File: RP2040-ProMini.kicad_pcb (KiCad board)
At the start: 2 copper layers, 17.8 x 33 mm, 6 parts, among them J1 CONN_L, J2 CONN_R, J3 CONN_R2, J4 CONN_R3, J5 CONN_U, U1 RP2040

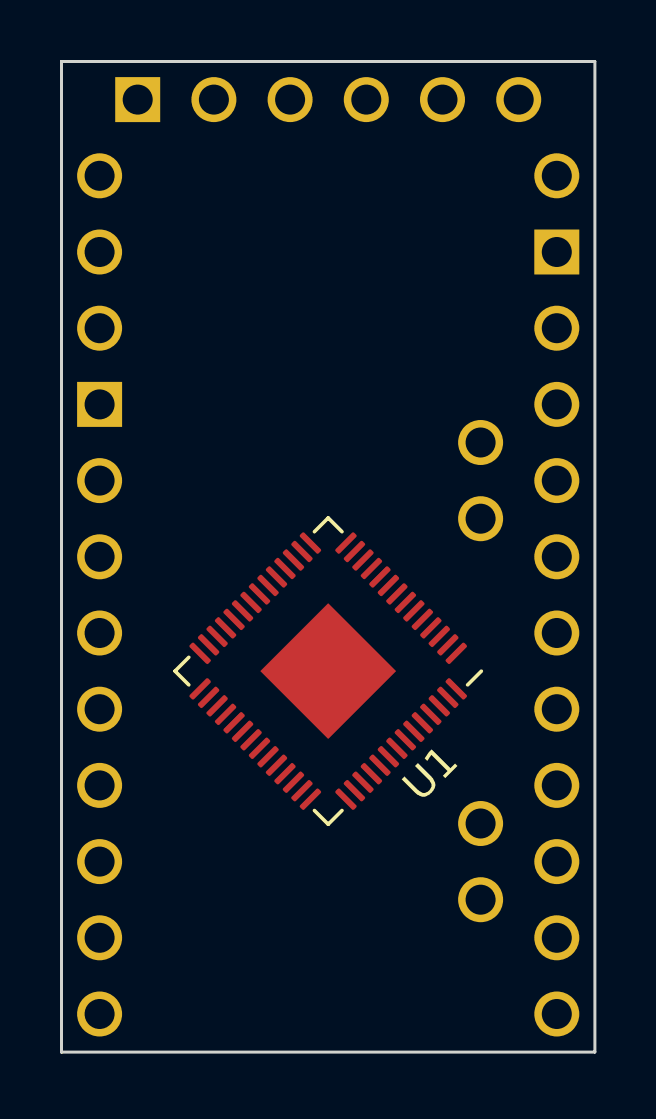
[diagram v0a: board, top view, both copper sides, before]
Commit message: Added basic power input
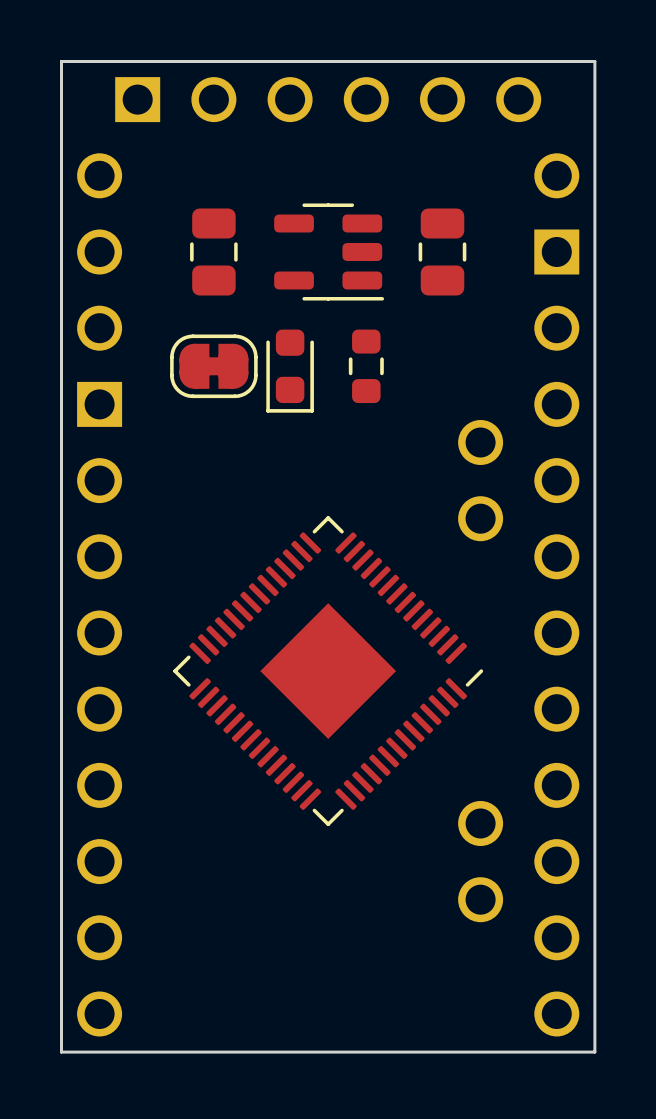
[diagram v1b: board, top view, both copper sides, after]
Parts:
- added C1: 10uF, Capacitor_SMD:C_0805_2012Metric, F.Cu at (160.0, 100.3)
- added C2: 10uF, Capacitor_SMD:C_0805_2012Metric, F.Cu at (152.4, 100.3)
- added D1: RED, LED_SMD:LED_0603_1608Metric, F.Cu at (154.9, 104.1)
- added JP1: EXT_POWER, Jumper:SolderJumper-2_P1.3mm_Bridged_RoundedPad1.0x1.5mm, F.Cu at (152.4, 104.1)
- added R1: 10k, Resistor_SMD:R_0603_1608Metric, F.Cu at (157.5, 104.1)
- added U2: MIC5205-3.3YM5, Package_TO_SOT_SMD:SOT-23-5, F.Cu at (156.2, 100.3)

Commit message: Added whole bunch of things
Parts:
- added C10: 100nF, Capacitor_SMD:C_0402_1005Metric, F.Cu at (151.1, 110.5)
- added C11: 2.2uF, Capacitor_SMD:C_0603_1608Metric, F.Cu at (158.7, 119.4)
- added C12: 2.2uF, Capacitor_SMD:C_0603_1608Metric, F.Cu at (151.1, 123.2)
- added C3: 100nF, Capacitor_SMD:C_0402_1005Metric, F.Cu at (151.1, 125.7)
- added C4: 100nF, Capacitor_SMD:C_0402_1005Metric, F.Cu at (157.5, 106.7)
- added C5: 100nF, Capacitor_SMD:C_0402_1005Metric, F.Cu at (151.1, 109.2)
- added C6: 100nF, Capacitor_SMD:C_0402_1005Metric, F.Cu at (157.5, 120.7)
- added C7: 100nF, Capacitor_SMD:C_0402_1005Metric, F.Cu at (156.2, 120.7)
- added C8: 100nF, Capacitor_SMD:C_0402_1005Metric, F.Cu at (151.1, 115.6)
- added C9: 100nF, Capacitor_SMD:C_0402_1005Metric, F.Cu at (158.8, 106.7)
- added D2: RED, LED_SMD:LED_0603_1608Metric, F.Cu at (152.4, 120.7)
- added Q1: AO3400A, Package_TO_SOT_SMD:SOT-23, F.Cu at (152.4, 118.1)
- added R2: 10k, Resistor_SMD:R_0402_1005Metric, F.Cu at (158.8, 102.9)
- added R3: 10k, Resistor_SMD:R_0402_1005Metric, F.Cu at (160.0, 102.9)
- added R4: 10k, Resistor_SMD:R_0402_1005Metric, F.Cu at (161.3, 102.9)
- added R5: 10k, Resistor_SMD:R_0402_1005Metric, F.Cu at (151.1, 102.9)
- added R6: 10k, Resistor_SMD:R_0402_1005Metric, F.Cu at (154.9, 120.7)
- added U3: W25Q128JVS, Package_SO:SOIC-8_5.23x5.23mm_P1.27mm, F.Cu at (157.5, 124.5)
- added Y1: 12MHz, Crystal:Crystal_SMD_3225-4Pin_3.2x2.5mm, F.Cu at (152.4, 106.7)
- R1: footprint Resistor_SMD:R_0603_1608Metric -> Resistor_SMD:R_0402_1005Metric
- moved J4 2.54 mm to (161.3, 116.8)
- moved D1 1.80 mm to (156.2, 102.9)
- moved JP1 1.80 mm to (153.7, 102.9)
- moved C1 1.27 mm to (160.0, 99.1), turned to -90 degrees
- moved C2 1.27 mm to (152.4, 99.1)
- moved R1 1.27 mm to (157.5, 102.9)
- moved U1 1.27 mm to (156.2, 113.0)
- moved U2 1.27 mm to (156.2, 99.1)
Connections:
- C2 pad 1: VCC -> +3.3V
- J2 pad 4: VCC -> +3.3V
- J5 pad 2: unconnected-(J5-Pin_2-Pad2) -> USB_DP
- J5 pad 4: unconnected-(J5-Pin_4-Pad4) -> USB_DM
- J5 pad 5: unconnected-(J5-Pin_5-Pad5) -> SWCLK
- J5 pad 6: unconnected-(J5-Pin_6-Pad6) -> SWD
- JP1 pad 2: VCC -> +3.3V
- U1 pad 1: Net-(U1-IOVDD-Pad1) -> +3.3V
- U1 pad 10: Net-(U1-IOVDD-Pad1) -> +3.3V
- U1 pad 19: unconnected-(U1-TESTEN-Pad19) -> GND
- U1 pad 20: unconnected-(U1-XIN-Pad20) -> XIN
- U1 pad 21: unconnected-(U1-XOUT-Pad21) -> XOUT
- U1 pad 22: Net-(U1-IOVDD-Pad1) -> +3.3V
- U1 pad 23: Net-(U1-DVDD-Pad23) -> +1V1
- U1 pad 24: unconnected-(U1-SWCLK-Pad24) -> SWCLK
- U1 pad 25: unconnected-(U1-SWD-Pad25) -> SWD
- U1 pad 26: unconnected-(U1-RUN-Pad26) -> RESET
- U1 pad 33: Net-(U1-IOVDD-Pad1) -> +3.3V
- U1 pad 42: Net-(U1-IOVDD-Pad1) -> +3.3V
- U1 pad 43: unconnected-(U1-ADC_AVDD-Pad43) -> +3.3V
- U1 pad 44: unconnected-(U1-VREG_IN-Pad44) -> +3.3V
- U1 pad 45: unconnected-(U1-VREG_VOUT-Pad45) -> +1V1
- U1 pad 46: unconnected-(U1-USB_DM-Pad46) -> USB_DM
- U1 pad 47: unconnected-(U1-USB_DP-Pad47) -> USB_DP
- U1 pad 48: unconnected-(U1-USB_VDD-Pad48) -> +3.3V
- U1 pad 49: Net-(U1-IOVDD-Pad1) -> +3.3V
- U1 pad 50: Net-(U1-DVDD-Pad23) -> +1V1
- U1 pad 51: unconnected-(U1-QSPI_SD3-Pad51) -> QSPI_SD3
- U1 pad 52: unconnected-(U1-QSPI_SCLK-Pad52) -> QSPI_SCLK
- U1 pad 53: unconnected-(U1-QSPI_SD0-Pad53) -> QSPI_SD0
- U1 pad 54: unconnected-(U1-QSPI_SD2-Pad54) -> QSPI_SD2
- U1 pad 55: unconnected-(U1-QSPI_SD1-Pad55) -> QSPI_SD1
- U1 pad 56: unconnected-(U1-QSPI_SS-Pad56) -> QSPI_SS

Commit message: Removed 2-pin connector. Routed power traces and fills. Started to route traces.
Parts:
- removed the C7 at (156.2, 120.7)
- removed the C9 at (158.8, 106.7)
- removed the J4 at (161.3, 116.8)
- added JP1: EXT_LED, Jumper:SolderJumper-2_P1.3mm_Bridged_RoundedPad1.0x1.5mm, B.Cu at (156.2, 120.0)
- JP2: renamed from JP1; moved to B.Cu
- moved R1 4.26 mm to (158.8, 118.7)
- moved D1 3.86 mm to (156.2, 120.0), turned to 180 degrees
- moved R5 3.81 mm to (153.7, 102.9), turned to -90 degrees
- moved C6 3.18 mm to (160.0, 118.7)
- moved C5 2.85 mm to (161.3, 118.1)
- moved JP2 2.54 mm to (156.2, 102.9), turned to -90 degrees
- moved R6 1.27 mm to (152.4, 102.9)
- moved Y1 0.90 mm to (153.0, 106.0)
- moved C3 0.64 mm to (158.1, 106.7)
- moved C9 0.64 mm to (159.4, 99.1)
- moved Q1 0.64 mm to (152.4, 118.7)
- moved C1 0.63 mm to (151.8, 123.2), turned to 90 degrees
- moved C10 0.63 mm to (153.0, 99.1)
- moved C2 0.63 mm to (151.8, 125.7), turned to -90 degrees
- moved U1 0.63 mm to (157.5, 123.8)
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- renumbered C12 to C1, C2 to C10, C3 to C2, C4 to C3, C5 to C4, C11 to C5, C10 to C7, C1 to C9, D2 to D1, D1 to D2, J5 to J2, J2 to J4, R6 to R1, R4 to R2, R2 to R3, R3 to R4, R1 to R5, R5 to R6, U3 to U1, U1 to U2, U2 to U3
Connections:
- net +3.3V renamed +3V3
- net D18_A4_SDA renamed D18_SDA
- net D19_A5_SCL renamed D19_SCL
- J2 pad 2: USB_DP -> USB_DN
- J2 pad 4: USB_DM -> USB_DP
- Q1 pad 1: D13_SCK -> Net-(JP1-B)
- U2 pad 46: USB_DM -> USB_DN
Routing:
- net +3V3: track 0.00 -> 27.6 mm, vias 0 -> 14
- net USB_DN: track 0.00 -> 24.2 mm, vias 0 -> 1
- net USB_DP: track 0.00 -> 24.2 mm, vias 0 -> 1
- net +1V1: track 0.00 -> 18.0 mm, vias 0 -> 4
- net GND: track 0.00 -> 17.8 mm, vias 0 -> 20
- net VIN: track 0.00 -> 7.78 mm, vias 0 -> 3
- net XIN: track 0.00 -> 5.90 mm
- net Net-(Q1-D): track 0.00 -> 5.63 mm
- net Net-(JP1-B): track 0.00 -> 5.40 mm, vias 0 -> 1
- net Net-(D2-A): track 0.00 -> 4.53 mm, vias 0 -> 1
- net XOUT: track 0.00 -> 4.41 mm
- net Net-(D1-K): track 0.00 -> 2.07 mm
- net Net-(D2-K): track 0.00 -> 1.96 mm
- added copper zone on In2.Cu, net +3V3
- added copper zone on B.Cu, net GND
- added copper zone on F.Cu, net GND
- added copper zone on In1.Cu, net GND
- added copper zone on In2.Cu, net VIN
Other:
- copper layers 2 -> 4

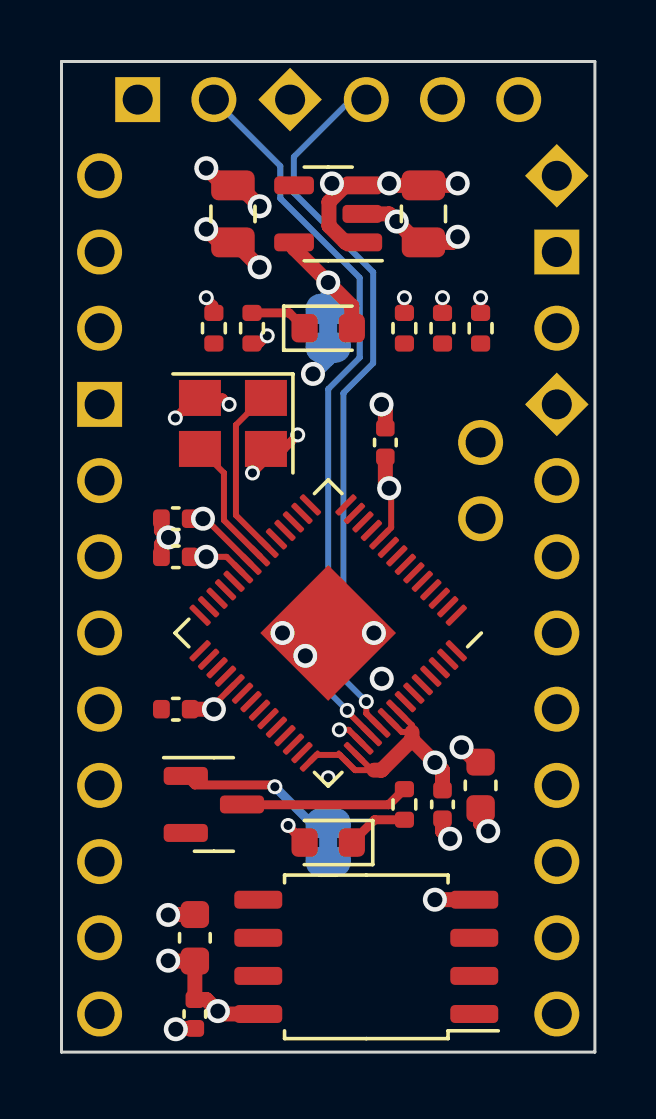
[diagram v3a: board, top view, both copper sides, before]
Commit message: Routed few more traces
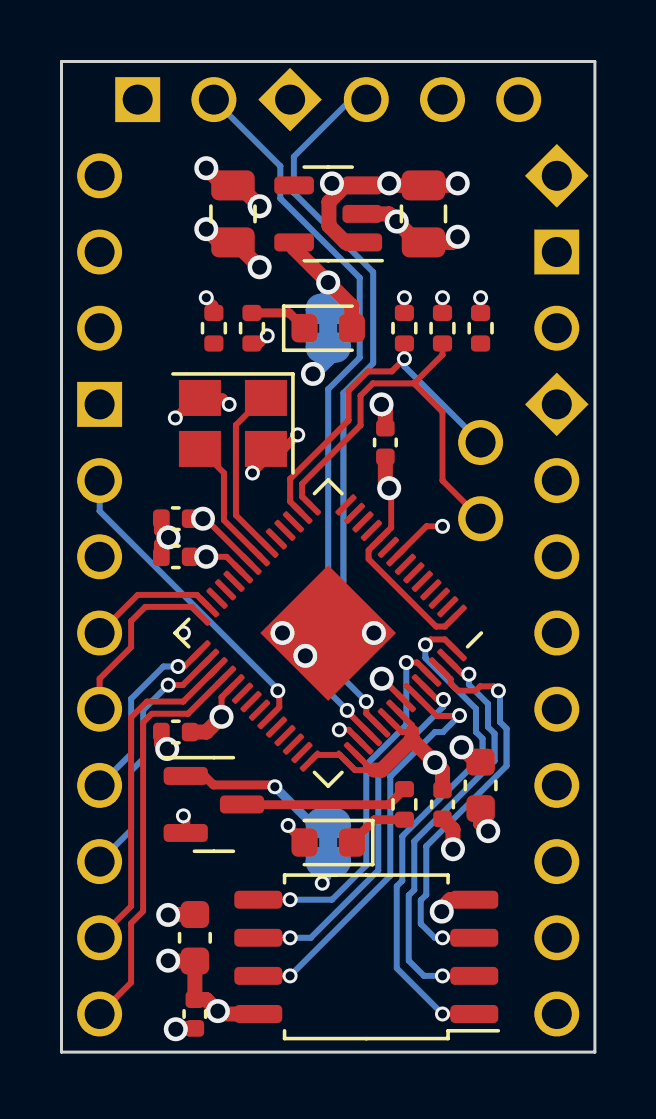
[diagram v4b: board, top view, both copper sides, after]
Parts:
- moved C8 0.76 mm to (151.1, 116.3)
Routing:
- net D13_SCK: track 0.00 -> 24.1 mm, vias 0 -> 2
- net QSPI_SS: track 0.00 -> 17.2 mm, vias 0 -> 2
- net QSPI_SD1: track 0.00 -> 14.4 mm, vias 0 -> 2
- net QSPI_SD3: track 0.00 -> 14.1 mm, vias 0 -> 2
- net D9: track 0.00 -> 13.7 mm
- net D18_SDA: track 0.00 -> 13.7 mm
- net QSPI_SD2: track 0.00 -> 13.5 mm, vias 0 -> 2
- net QSPI_SCLK: track 0.00 -> 12.4 mm, vias 0 -> 2
- net QSPI_SD0: track 0.00 -> 12.4 mm, vias 0 -> 2
- net D19_SCL: track 0.00 -> 11.7 mm, vias 0 -> 1
- net D8: track 0.00 -> 11.3 mm
- net D2: track 0.00 -> 10.6 mm, vias 0 -> 1
- net D7: track 0.00 -> 8.53 mm, vias 0 -> 1
- net D6: track 0.00 -> 6.28 mm, vias 0 -> 1
- net D5: track 0.00 -> 5.98 mm
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
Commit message: Finished routing of the board.
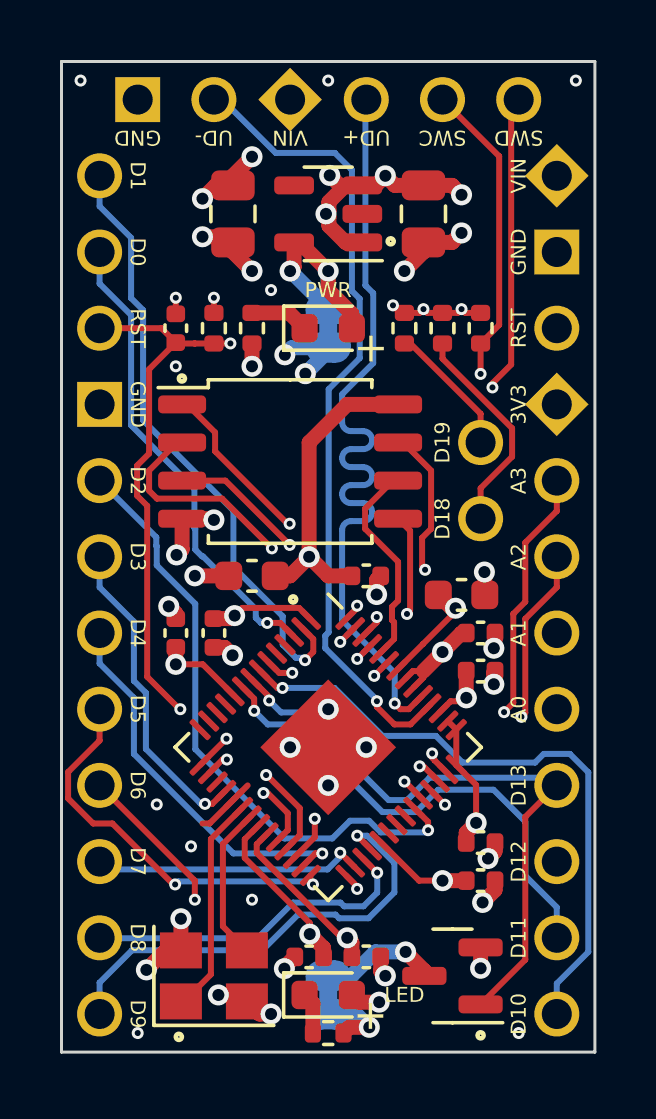
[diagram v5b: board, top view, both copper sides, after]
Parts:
- added C11: 100nF, Capacitor_SMD:C_0402_1005Metric, F.Cu at (161.3, 121.3)
- added C12: 10uF, Capacitor_SMD:C_0805_2012Metric, F.Cu at (159.4, 99.1)
- added C13: 100nF, Capacitor_SMD:C_0402_1005Metric, F.Cu at (151.1, 102.9)
- added C14: 10uF, Capacitor_SMD:C_0805_2012Metric, F.Cu at (153.0, 99.1)
- C10, C9: value 10uF -> 100nF; footprint Capacitor_SMD:C_0805_2012Metric -> Capacitor_SMD:C_0402_1005Metric
- JP1: value EXT_LED -> CUT_LED
- JP2: value EXT_POWER -> CUT_VIN
- moved Y1 18.4 mm to (152.4, 124.5), turned to 0 degrees
- moved U1 16.7 mm to (154.9, 107.3), turned to 0 degrees
- moved C2 15.7 mm to (157.5, 111.1), turned to 0 degrees
- moved C9 15.4 mm to (161.3, 114.3), turned to 0 degrees
- moved C7 14.8 mm to (157.5, 123.8), turned to 0 degrees
- moved C10 14.0 mm to (152.4, 113.0), turned to -90 degrees
- moved C1 12.2 mm to (153.7, 111.1), turned to 180 degrees
- moved C4 10.9 mm to (161.3, 113.0), turned to 0 degrees
- moved Q1 9.79 mm to (160.4, 124.5), turned to 180 degrees
- moved C3 9.44 mm to (151.1, 113.0)
- moved C8 8.71 mm to (155.6, 123.8)
- moved R1 8.03 mm to (156.2, 126.4), turned to 0 degrees
- moved C5 6.38 mm to (160.7, 111.8), turned to 0 degrees
- moved D1 5.08 mm to (156.2, 125.1), turned to 0 degrees
- moved JP1 5.08 mm to (156.2, 125.1), turned to -90 degrees
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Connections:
- net D11_COPI renamed D11_MOSI
- net D12_CIPO renamed D12_MISO
- C9 pad 1: VIN -> +1V1
- JP1 pad 1: D13_SCK -> Net-(JP1-A)
- Q1 pad 1: Net-(JP1-B) -> D13_SCK
- Q1 pad 3: Net-(Q1-D) -> Net-(JP1-A)
- R1 pad 2: Net-(Q1-D) -> Net-(JP1-B)
- R5 pad 1: Net-(D2-K) -> +3V3
- R5 pad 2: GND -> RESET
- R6 pad 1: +3V3 -> Net-(D2-K)
- R6 pad 2: RESET -> GND
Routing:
- net RESET: track 0.00 -> 37.0 mm, vias 0 -> 3
- net SWCLK: track 0.00 -> 36.9 mm, vias 0 -> 2
- net SWD: track 0.00 -> 36.7 mm, vias 0 -> 2
- net +3V3: track 33.0 -> 67.7 mm, vias 14 -> 16
- net D10_SS: track 0.00 -> 21.1 mm, vias 0 -> 1
- net D1_TX: track 0.00 -> 20.5 mm, vias 0 -> 1
- net D11_MOSI: track 0.00 -> 16.4 mm, vias 0 -> 1
- net D0_RX: track 0.00 -> 15.9 mm, vias 0 -> 1
- net D12_MISO: track 0.00 -> 13.5 mm, vias 0 -> 1
- net D17_A3: track 0.00 -> 12.3 mm, vias 0 -> 2
- net D19_SCL: track 11.7 -> 23.0 mm
- net D16_A2: track 0.00 -> 10.8 mm, vias 0 -> 2
- net D3: track 0.00 -> 10.6 mm, vias 0 -> 1
- net D18_SDA: track 13.7 -> 24.1 mm, vias 0 -> 1
- net D2: track 10.6 -> 20.7 mm
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- added copper zone on In1.Cu, net +3V3
- added copper zone on In2.Cu, net GND
- added copper zone on In1.Cu, net VIN
- removed copper zone on In2.Cu, net +3V3
- removed copper zone on In1.Cu, net GND
- removed copper zone on In2.Cu, net VIN
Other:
- board text added: "${COMPANY}"
- board text added: "${TITLE}"
- board text added: "+"
- board text added: "3V3"
- board text added: "A0"
- board text added: "A1"
- board text added: "A2"
- board text added: "A3"
- board text added: "CUT_LED"
- board text added: "CUT_VIN"
- board text added: "D0"
- board text added: "D1"
- board text added: "D10"
- board text added: "D11"
- board text added: "D12"
- board text added: "D13"
- board text added: "D14"
- board text added: "D15"
- board text added: "D16"
- board text added: "D17"
- board text added: "D18"
- board text added: "D19"
- board text added: "D2"
- board text added: "D3"
- board text added: "D4"
- board text added: "D5"
- board text added: "D6"
- board text added: "D7"
- board text added: "D8"
- board text added: "D9"
- board text added: "GND"
- board text added: "LED"
- board text added: "MISO"
- board text added: "MOSI"
- board text added: "PWR"
- board text added: "RST"
- board text added: "RX"
- board text added: "SCK"
- board text added: "SCL"
- board text added: "SDA"
- board text added: "SS"
- board text added: "SWC"
- board text added: "SWD"
- board text added: "TX"
- board text added: "UD+"
- board text added: "UD-"
- board text added: "VIN"

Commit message: Optimized routing a bit
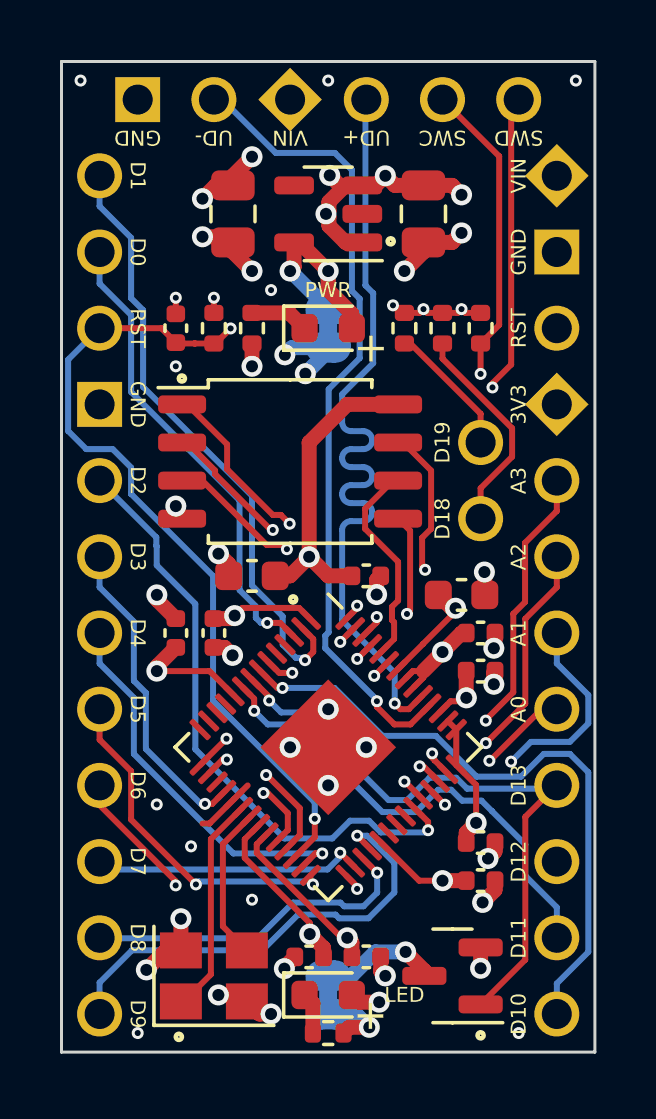
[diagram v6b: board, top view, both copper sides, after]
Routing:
- net +3V3: track 67.7 -> 58.2 mm
- net QSPI_SD1: track 11.8 -> 9.66 mm
- net SWD: track 36.7 -> 34.8 mm
- net SWCLK: track 36.9 -> 35.0 mm
- net D5: track 13.2 -> 11.5 mm
- net GND: track 23.5 -> 21.9 mm, vias 38 -> 37
- net RESET: track 37.0 -> 38.0 mm, vias 3 -> 2
- net D15_A1: track 9.99 -> 10.0 mm, vias 1 -> 2
- net D14_A0: track 6.95 -> 6.96 mm, vias 1 -> 2
